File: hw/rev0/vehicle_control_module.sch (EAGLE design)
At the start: 495 parts, among them IC1 SJA1105TELY, IC10 TJA1100HNZ, IC11 KSZ8061MNXI-TR, IC12 TJA1100HNZ, IC13 TLE9250XSJXUMA1, IC17 LP5907QMFX-3.3Q1, IC18 TLE9250XSJXUMA1, IC2 ATSAMV71Q21B-AABT, IC3 TJA1100HNZ, IC4 FT2232HL, IC5 TRS3232EQPWRQ1, IC6 SST26VF032BT-104I_SM, IC7 DS3231SN#, IC8 74HC7541D-Q100J, IC9 TPS62242DRVR, J10 5-2337992-3, J11 2301843-1, J12 1017505, J13 2301843-1, J15 693022010811, J2 2305018-2, J27 2041119-2, J3 1017505, J4 1017505, J5 1017505, J6 1017505, J7 1017505, J8 1017505, J9 1017505, U1 122-2920-GR, U2 LM63625, U3 TPS62007-Q1_DGS_10, Y1 NX3225SA-25MHZ-EXS00A-CS11338, Y3 ABM8AIG-12.000MHZ-1Z-T

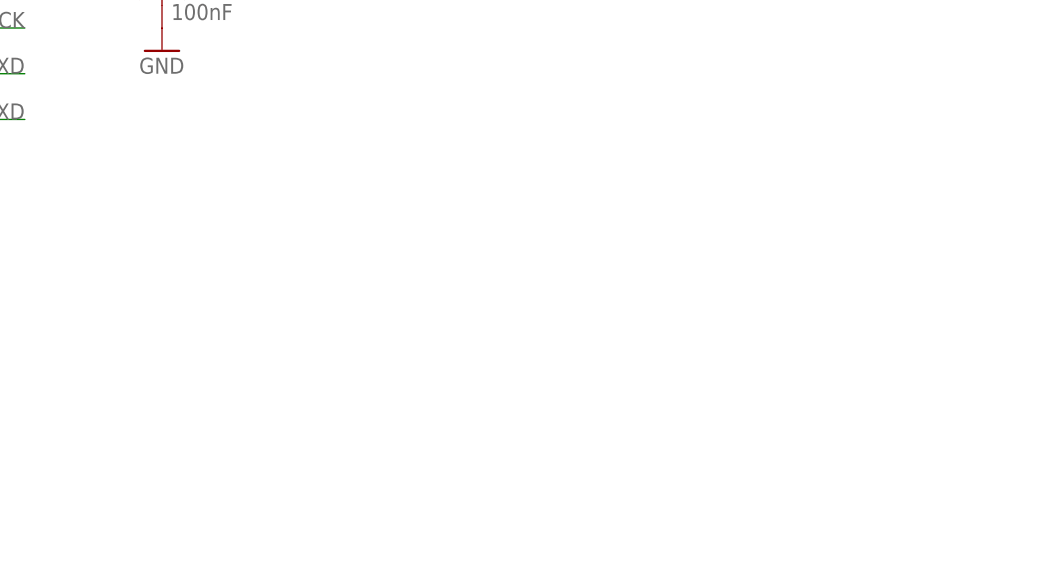
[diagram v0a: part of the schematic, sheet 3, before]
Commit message: Add missing oscillator, start to layout testtool board
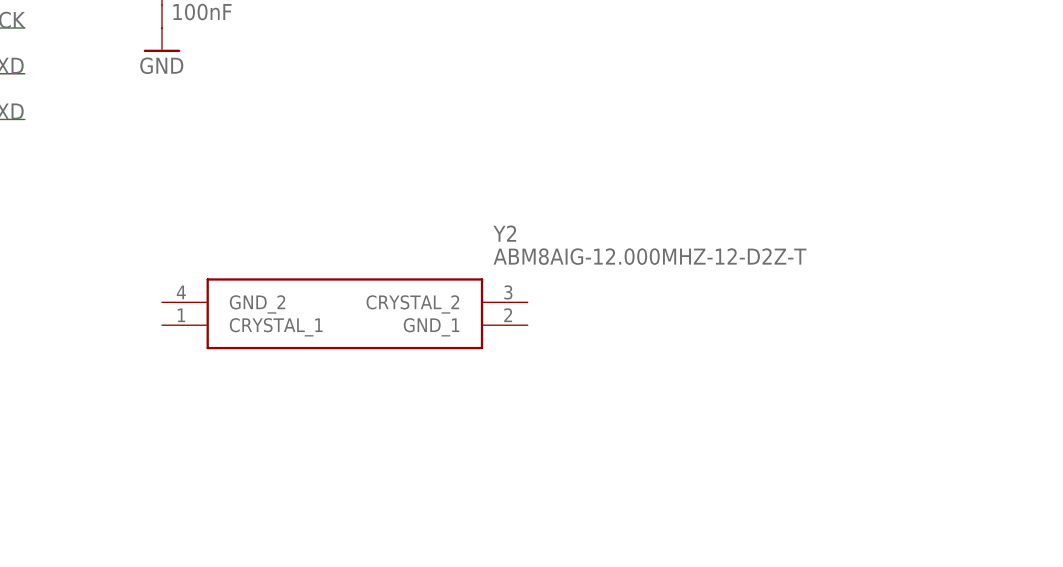
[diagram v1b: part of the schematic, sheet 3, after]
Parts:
- added Y2: ABM8AIG-12.000MHZ-12-D2Z-T, samacsys:ABM8AIG-12.000MHZ-12-D2Z-T
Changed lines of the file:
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@@
 <part name="R199" library="rcl" library_urn="urn:adsk.eagle:library:334" deviceset="R-US_" device="R0603" package3d_urn="urn:adsk.eagle:package:23555/3" value="10k"/>
 <part name="GND313" library="supply1" library_urn="urn:adsk.eagle:library:371" deviceset="GND" device=""/>
+<part name="Y2" library="samacsys" deviceset="ABM8AIG-12.000MHZ-12-D2Z-T" device=""/>
 </parts>
 <sheets>
@@
 <attribute name="VALUE" x="373.38" y="175.26" size="1.778" layer="96"/>
 </instance>
+<instance part="Y2" gate="G$1" x="292.1" y="66.04" smashed="yes">
+<attribute name="NAME" x="328.93" y="73.66" size="1.778" layer="95" align="center-left"/>
+<attribute name="VALUE" x="328.93" y="71.12" size="1.778" layer="96" align="center-left"/>
+</instance>
 </instances>
